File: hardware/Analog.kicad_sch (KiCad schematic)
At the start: 59 parts, among them J4 AudioJack3, J5 AudioJack3, U10 LTC6373, U11 TAC5212, U9 OPA376xxDBV

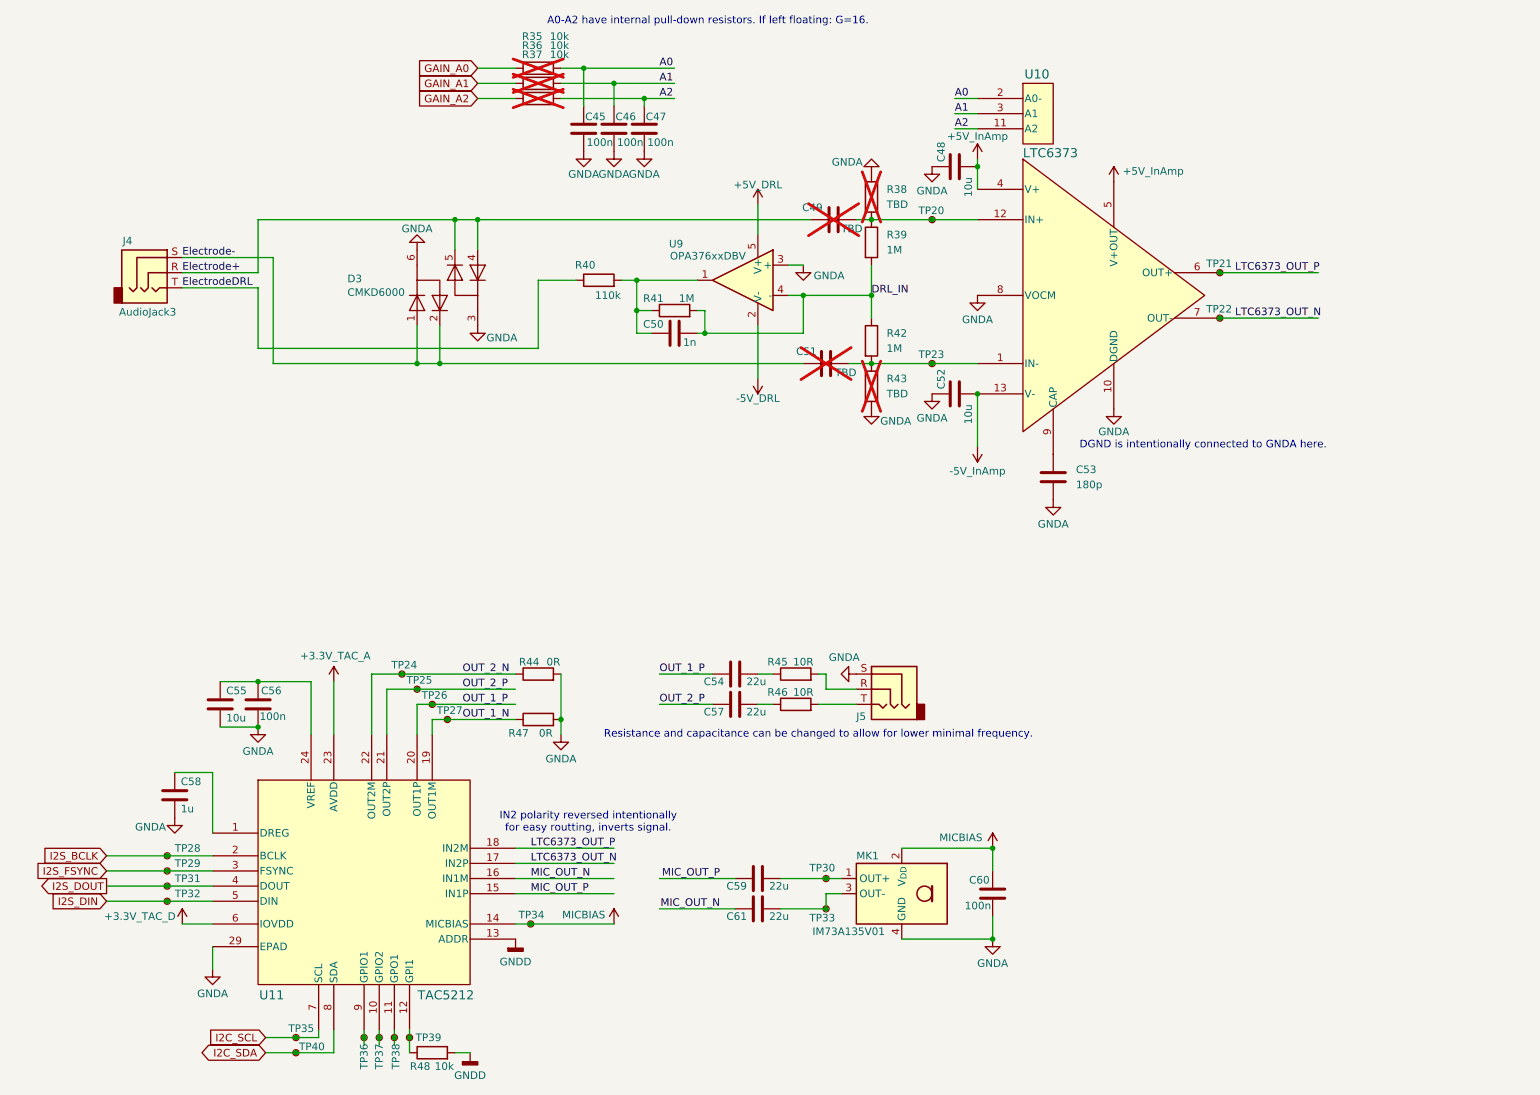
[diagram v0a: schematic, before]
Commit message: Changed Pinheader and found a Problem with V0CM.
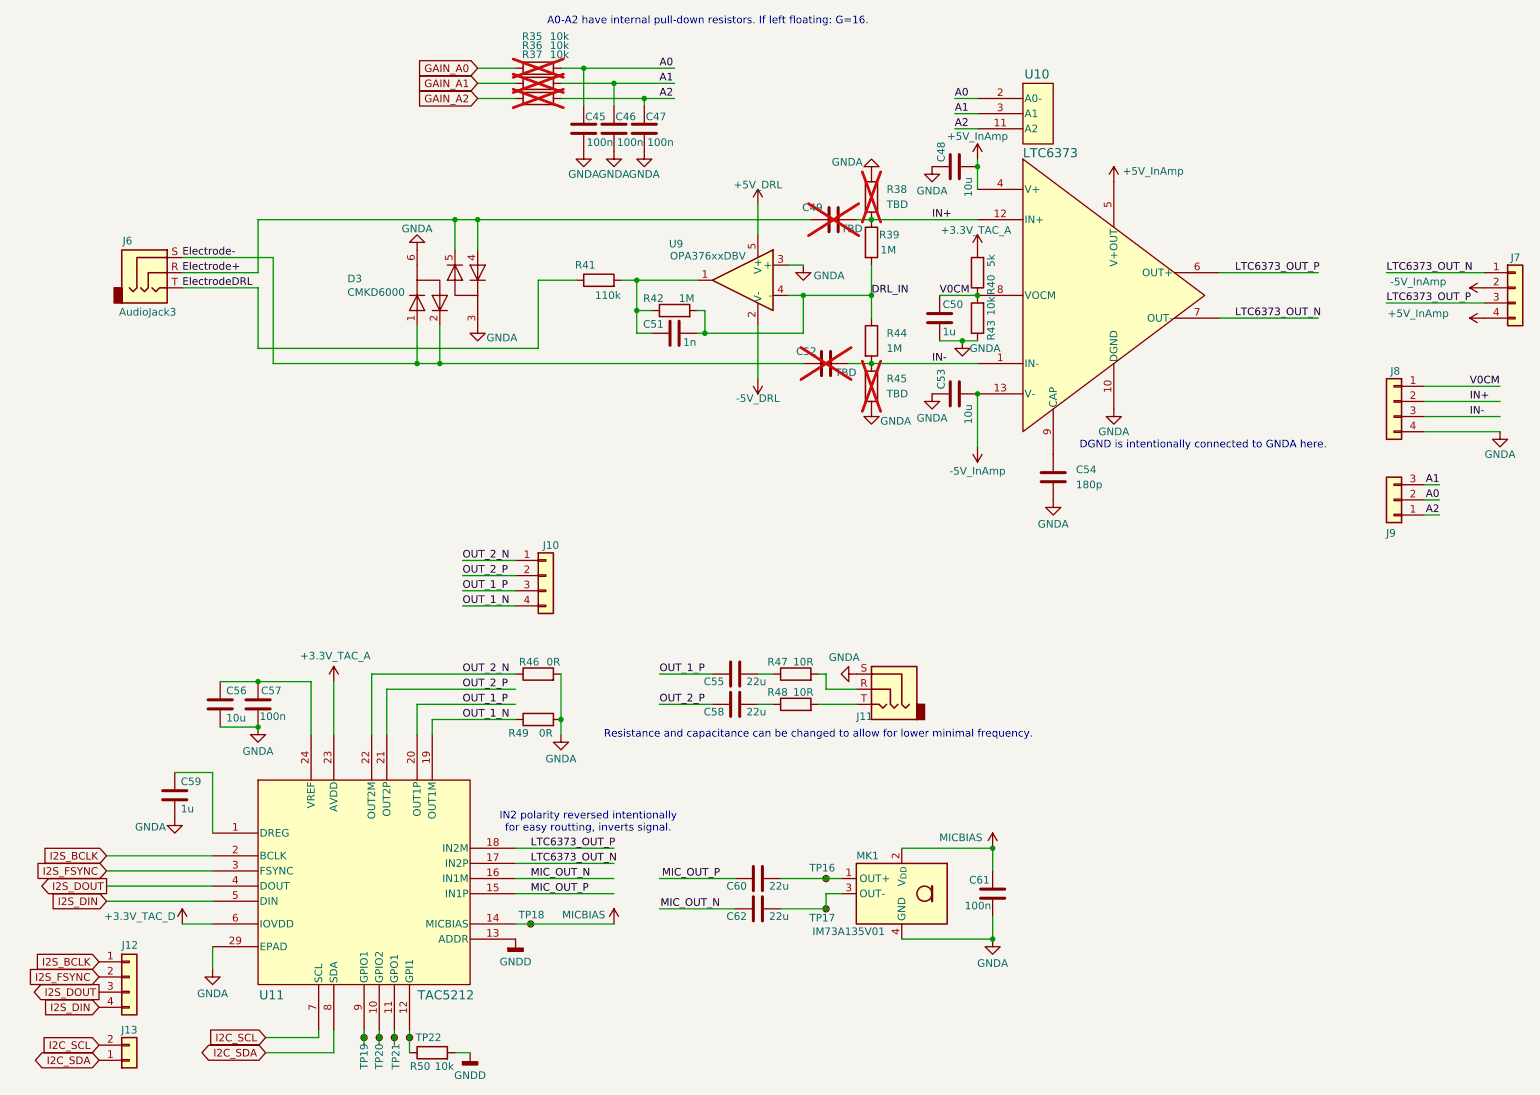
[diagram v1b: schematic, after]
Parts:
- removed TP20, TP21, TP22, TP23, TP24, TP25, TP26, TP27, TP28, TP29, TP31, TP32, TP35, TP40: TestPoint_Small, TestPoint:TestPoint_Loop_D2.60mm_Drill0.9mm_Beaded, symbol Connector:TestPoint_Small
- added C50: 1u, Capacitor_SMD:C_0603_1608Metric, symbol Device:C
- added J10, J12, J7, J8: PinHeader_01x04_2.54mm_Vertical, Connector_PinHeader_2.54mm:PinHeader_1x04_P2.54mm_Vertical, symbol PCM_PinHeader_Generic_2.54mm:PinHeader_01x04_2.54mm_Vertical
- added J13: PinHeader_01x02_2.54mm_Vertical, Connector_PinHeader_2.54mm:PinHeader_1x02_P2.54mm_Vertical, symbol PCM_PinHeader_Generic_2.54mm:PinHeader_01x02_2.54mm_Vertical
- added J9: PinHeader_01x03_2.54mm_Vertical, Connector_PinHeader_2.54mm:PinHeader_1x03_P2.54mm_Vertical, symbol PCM_PinHeader_Generic_2.54mm:PinHeader_01x03_2.54mm_Vertical
- added R40: 5k, Resistor_SMD:R_0603_1608Metric, symbol Device:R
- added R43: 10k, Resistor_SMD:R_0603_1608Metric, symbol Device:R
- renumbered C50 to C51, C51 to C52, C52 to C53, C53 to C54, C54 to C55, C55 to C56, C56 to C57, C57 to C58, C58 to C59, C59 to C60, C60 to C61, C61 to C62, J5 to J11, J4 to J6, R40 to R41, R41 to R42, R42 to R44, R43 to R45, R44 to R46, R45 to R47, R46 to R48, R47 to R49, R48 to R50, TP30 to TP16, TP33 to TP17, TP34 to TP18, TP36 to TP19, TP37 to TP20, TP38 to TP21, TP39 to TP22
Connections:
- net +3.3V_TAC_A: now also R40.2
- net +5V_InAmp: now also J7.4 (Pin_4)
- net -5V_InAmp: now also J7.2 (Pin_2)
- net A0: now also J9.2 (Pin_2)
- net A1: now also J9.3 (Pin_3)
- net A2: now also J9.1 (Pin_1)
- net GNDA: now also C50.2, J8.4 (Pin_4), R43.1; no longer U10.8 (VOCM)
- net I2C_SCL: now also J13.2 (Pin_2)
- net I2C_SDA: now also J13.1 (Pin_1)
- net I2S_BCLK: now also J12.1 (Pin_1)
- net I2S_DIN: now also J12.4 (Pin_4)
- net I2S_DOUT: now also J12.3 (Pin_3)
- net I2S_FSYNC: now also J12.2 (Pin_2)
- net LTC6373_OUT_N: now also J7.1 (Pin_1)
- net LTC6373_OUT_P: now also J7.3 (Pin_3)
- net OUT_1_N: now also J10.4 (Pin_4)
- net OUT_1_P: now also J10.3 (Pin_3)
- net OUT_2_N: now also J10.1 (Pin_1)
- net OUT_2_P: now also J10.2 (Pin_2)
- net IN-: now reaches C52.2, R44.2, R45.1, U10.1 (IN-)
- net IN-: now also J8.3 (Pin_3)
- net IN+: now reaches C49.2, R38.2, R39.1, U10.12 (IN+)
- net IN+: now also J8.2 (Pin_2)
- new net V0CM: C50.1, J8.1 (Pin_1), R40.1, R43.2, U10.8 (VOCM)

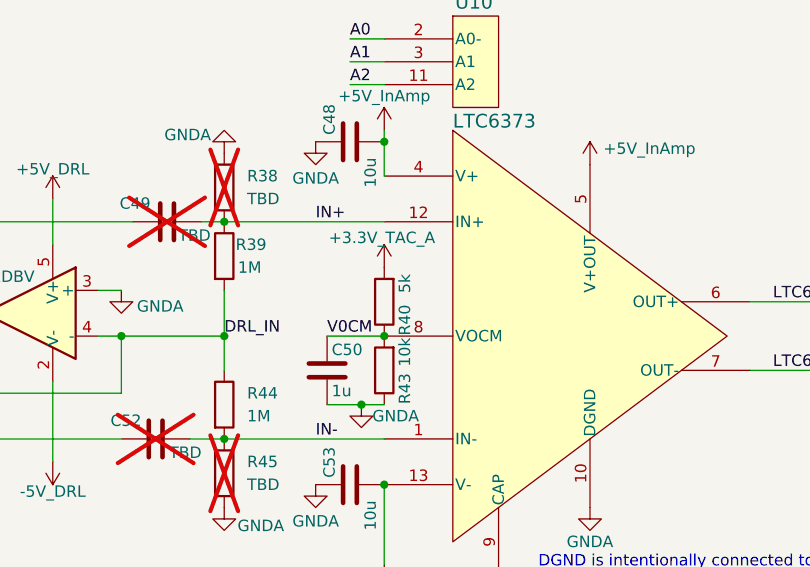
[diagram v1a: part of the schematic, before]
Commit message: Release: First PCB manufacturing batch. Fixed U10 thermal via short, exempted fiducials from solder mask margin override rule, adjusted R22 label, and updated all manufacturing files.
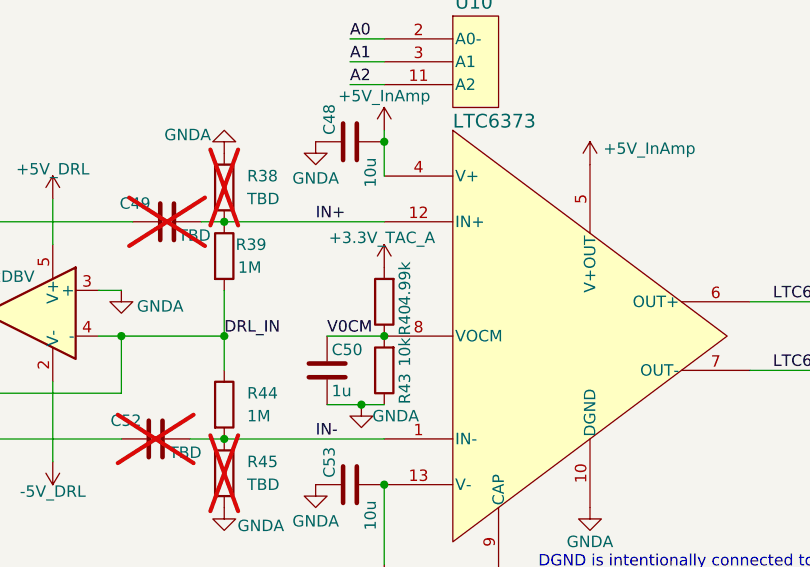
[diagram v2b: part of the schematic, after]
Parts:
- R40: value 5k -> 4.99k; MPN CRCW0603????? -> CRCW06034K99FKEA; Supplier ? -> Lager; Supplier_PN ? -> T02
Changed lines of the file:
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@@
 			)
 		)
-		(property "Value" "5k"
+		(property "Value" "4.99k"
 			(at 175.006 56.388 90)
 			(show_name no)
@@
 			)
 		)
-		(property "MPN" "CRCW0603?????"
+		(property "MPN" "CRCW06034K99FKEA"
 			(at 172.72 58.42 0)
 			(hide yes)
@@
 			)
 		)
-		(property "Supplier" "?"
+		(property "Supplier" "Lager"
 			(at 172.72 58.42 0)
 			(hide yes)
@@
 			)
 		)
-		(property "Supplier_PN" "?"
+		(property "Supplier_PN" "T02"
 			(at 172.72 58.42 0)
 			(hide yes)

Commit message: BOM Update: Replace C48 and C53 with Mouser part GRM188R61C106MA73J and update all exports.
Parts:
- C48, C53: MPN GRM188R61C106KE15D -> GRM188R61C106MA73J; Supplier Lager -> Mouser; Supplier_PN T26 -> GRM188R61C106MA73J
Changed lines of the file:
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@@
 			)
 		)
-		(property "MPN" "GRM188R61C106KE15D"
+		(property "MPN" "GRM188R61C106MA73J"
 			(at 168.91 78.74 0)
 			(hide yes)
@@
 			)
 		)
-		(property "Supplier" "Lager"
+		(property "Supplier" "Mouser"
 			(at 168.91 78.74 0)
 			(hide yes)
@@
 			)
 		)
-		(property "Supplier_PN" "T26"
+		(property "Supplier_PN" "GRM188R61C106MA73J"
 			(at 168.91 78.74 0)
 			(hide yes)
@@
 			)
 		)
-		(property "MPN" "GRM188R61C106KE15D"
-			(at 168.91 40.64 0)
-			(hide yes)
-			(show_name no)
-			(do_not_autoplace no)
-			(effects
-				(font
-					(size 1.27 1.27)
-				)
-			)
-		)
-		(property "Supplier" "Lager"
-			(at 168.91 40.64 0)
-			(hide yes)
-			(show_name no)
-			(do_not_autoplace no)
-			(effects
-				(font
-					(size 1.27 1.27)
-				)
-			)
-		)
-		(property "Supplier_PN" "T26"
-			(at 168.91 40.64 0)
-			(hide yes)
+		(property "MPN" "GRM188R61C106MA73J"
+			(at 168.91 40.64 0)
+			(hide yes)
+			(show_name no)
+			(do_not_autoplace no)
+			(effects
+				(font
+					(size 1.27 1.27)
+				)
+			)
+		)
+		(property "Supplier" "Mouser"
+			(at 168.91 40.64 0)
+			(hide yes)
+			(show_name no)
+			(do_not_autoplace no)
+			(effects
+				(font
+					(size 1.27 1.27)
+				)
+			)
+		)
+		(property "Supplier_PN" "GRM188R61C106MA73J"
+			(at 168.91 40.64 0)
+			(hide yes)
